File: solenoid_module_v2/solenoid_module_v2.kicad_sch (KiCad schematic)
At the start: 10 parts, among them J1 1x5 2.54, J2 1x5 2.54, J3 1x2 5.08, J4 1x2 5.08, J5 Screw_Terminal_01x04, Q1 BC817, Q2 BC817, SW1 3way switch

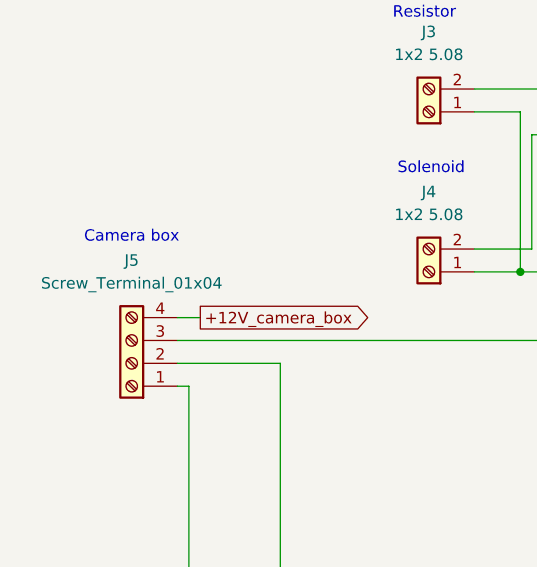
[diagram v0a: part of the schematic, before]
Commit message: Solenoid moduke new ver
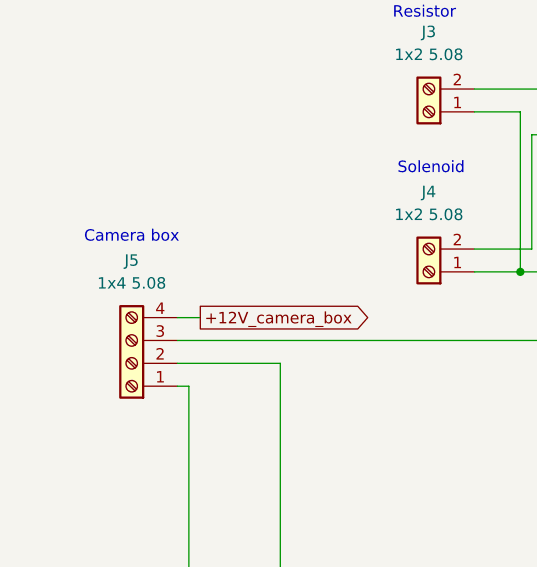
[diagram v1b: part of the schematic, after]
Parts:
- J5: value Screw_Terminal_01x04 -> 1x4 5.08; footprint (none) -> TerminalBlock_MetzConnect:TerminalBlock_MetzConnect_Type101_RT01604HBWC_1x04_P5.08mm_Horizontal; Manufacturer Part Number (none) -> TB0012-508-02GR; Mouser Part Number (none) -> 179-TB0012-508-02GR
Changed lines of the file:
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@@
 			)
 		)
-		(property "Value" "Screw_Terminal_01x04"
+		(property "Value" "1x4 5.08"
 			(at 58.42 73.66 0)
 			(effects
@@
 			)
 		)
-		(property "Footprint" ""
+		(property "Footprint" "TerminalBlock_MetzConnect:TerminalBlock_MetzConnect_Type101_RT01604HBWC_1x04_P5.08mm_Horizontal"
 			(at 58.42 82.55 0)
 			(effects
@@
 			(at 58.42 82.55 0)
 			(effects
+				(font
+					(size 1.27 1.27)
+				)
+				(hide yes)
+			)
+		)
+		(property "Manufacturer Part Number" "TB0012-508-02GR"
+			(at 58.42 82.55 0)
+			(effects
+				(font
+					(size 1.27 1.27)
+				)
+				(hide yes)
+			)
+		)
+		(property "Mouser Part Number" "179-TB0012-508-02GR"
+			(at 58.42 82.55 0)
+			(effects
